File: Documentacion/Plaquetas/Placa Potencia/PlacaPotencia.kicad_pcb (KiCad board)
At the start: 2 copper layers, 31 parts, among them J1 Conn_01x02_Male, Q1 IRF4905, Q2 IRFZ44N, Q3 IRF4905, Q4 IRFZ44N, Q5 BC337, Q6 BC337, U2 MCP1407, U3 MCP1407

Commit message: Power PCB Routed
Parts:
- added C_MCP1: 10n, Capacitor_THT:C_Rect_L7.5mm_W6.5mm_P5.00mm, F.Cu at (133.0, 44.5)
- added C_MCP2: 10n, Capacitor_THT:C_Rect_L7.5mm_W6.5mm_P5.00mm, F.Cu at (234.0, 63.0)
- moved BORNERA3 70.4 mm to (129.5, 83.5), turned to 180 degrees
- moved BORNERA2 68.9 mm to (129.5, 78.0), turned to 180 degrees
- moved PELTIER1 36.6 mm to (187.5, 45.0)
- moved C4 35.6 mm to (130.0, 67.0), turned to 180 degrees
- moved R22 30.8 mm to (209.0, 89.0), turned to 270 degrees
- moved R2 30.6 mm to (130.1, 63.0), turned to 180 degrees
- moved D1 26.4 mm to (196.5, 82.5), turned to 0 degrees
- moved R14 21.8 mm to (141.0, 60.1)
- moved Q4 21.5 mm to (151.5, 52.5)
- moved Q5 21.5 mm to (142.5, 54.5)
- moved R21 20.6 mm to (143.0, 70.5)
- moved U2 20.2 mm to (130.5, 53.0), turned to 90 degrees
- moved D3 20.0 mm to (173.5, 82.5), turned to 180 degrees
- moved D4 16.6 mm to (156.0, 57.0), turned to 0 degrees
- moved D2 14.7 mm to (220.5, 69.5)
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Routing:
- net GND: track 225.6 -> 353.7 mm, vias 0 -> 2
- net PWM_FRIO: track 126.6 -> 21.0 mm, vias 1 -> 0
- net PMOS_FRIO: track 92.0 -> 22.7 mm, vias 1 -> 2
- net PWM_CALOR: track 86.2 -> 130.6 mm, vias 1 -> 2
- net PMOS_CALOR: track 98.5 -> 131.4 mm, vias 1 -> 2
- net Net-(R22-Pad2): track 35.0 -> 64.1 mm
- net Net-(Q2-Pad1): track 54.1 -> 31.0 mm
- net Net-(Q1-Pad1): track 165.6 -> 184.3 mm, vias 1 -> 2
- net Net-(C2-Pad1): track 30.1 -> 44.1 mm
- net Net-(Q3-Pad1): track 137.6 -> 123.8 mm
- net VCC: track 522.7 -> 509.4 mm
- net Net-(C1-Pad1): track 35.2 -> 44.5 mm
- net Net-(R21-Pad2): track 33.7 -> 41.5 mm
- net Net-(Q4-Pad1): track 26.4 -> 21.5 mm
- net Net-(D1-Pad2): track 39.6 -> 43.2 mm
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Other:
- board outline added: 145 x 70 mm

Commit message: Power PCB revised
Minor changes in size and vias
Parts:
- moved J1 70.1 mm to (75.0, 42.5)
- moved R22 31.3 mm to (204.5, 58.0)
- moved R11 7.50 mm to (144.0, 82.5)
- moved BORNERA2 5.50 mm to (135.0, 78.0)
- moved BORNERA3 5.50 mm to (135.0, 83.5)
- moved C2 5.50 mm to (184.0, 69.5)
- moved C4 5.50 mm to (135.5, 67.0)
- moved C_MCP1 5.50 mm to (138.5, 44.5)
- moved D3 5.50 mm to (179.0, 82.5)
- moved D4 5.50 mm to (161.5, 57.0)
- moved L2 5.50 mm to (164.0, 69.5)
- moved Q3 5.50 mm to (153.5, 83.0)
- moved Q4 5.50 mm to (157.0, 52.5)
- moved Q5 5.50 mm to (148.0, 54.5)
- moved R14 5.50 mm to (146.5, 60.1)
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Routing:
- net Net-(Q2-Pad1): track 31.0 -> 4.50 mm
- net GND: track 353.7 -> 369.7 mm, vias 2 -> 0
- net Net-(R22-Pad2): track 64.1 -> 52.6 mm, vias 0 -> 1
- net PMOS_CALOR: track 131.4 -> 125.1 mm, vias 2 -> 1
- net Net-(Q3-Pad1): track 123.8 -> 118.3 mm
- net PWM_CALOR: track 130.6 -> 125.1 mm, vias 2 -> 1
- net VCC: track 509.4 -> 504.9 mm
- net Net-(C2-Pad1): track 44.1 -> 45.5 mm
- net Net-(Q1-Pad1): track 184.3 -> 183.5 mm, vias 2 -> 1
- net PMOS_FRIO: track 22.7 -> 22.3 mm, vias 2 -> 1

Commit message: Power PCB footprints updated
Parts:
- removed BORNERA2, BORNERA3: Screw_Terminal_01x02, Connector_PinHeader_2.54mm:PinHeader_1x02_P2.54mm_Vertical
- added C10: 4.7u, Capacitor_THT:C_Rect_L29.0mm_W9.1mm_P27.50mm_MKT, F.Cu at (21.8, 163.8)
- added C11: 4.7u, Capacitor_THT:C_Rect_L29.0mm_W9.1mm_P27.50mm_MKT, F.Cu at (84.7, 131.8)
- added C12: 4.7u, Capacitor_THT:C_Rect_L29.0mm_W9.1mm_P27.50mm_MKT, F.Cu at (21.8, 174.4)
- added C13: 4.7u, Capacitor_THT:C_Rect_L29.0mm_W9.1mm_P27.50mm_MKT, F.Cu at (53.2, 153.1)
- added C14: 4.7u, Capacitor_THT:C_Rect_L29.0mm_W9.1mm_P27.50mm_MKT, F.Cu at (84.7, 142.5)
- added C15: 4.7u, Capacitor_THT:C_Rect_L29.0mm_W9.1mm_P27.50mm_MKT, F.Cu at (53.2, 163.8)
- added C16: 4.7u, Capacitor_THT:C_Rect_L29.0mm_W9.1mm_P27.50mm_MKT, F.Cu at (53.2, 174.4)
- added C5: 4.7u, Capacitor_THT:C_Rect_L29.0mm_W9.1mm_P27.50mm_MKT, F.Cu at (21.8, 131.8)
- added C6: 4.7u, Capacitor_THT:C_Rect_L29.0mm_W9.1mm_P27.50mm_MKT, F.Cu at (21.8, 142.5)
- added C7: 4.7u, Capacitor_THT:C_Rect_L29.0mm_W9.1mm_P27.50mm_MKT, F.Cu at (53.2, 131.8)
- added C8: 4.7u, Capacitor_THT:C_Rect_L29.0mm_W9.1mm_P27.50mm_MKT, F.Cu at (21.8, 153.1)
- added C9: 4.7u, Capacitor_THT:C_Rect_L29.0mm_W9.1mm_P27.50mm_MKT, F.Cu at (53.2, 142.5)
- added J2: Conn_01x10_Male, Connector_IDC:IDC-Header_2x05_P2.54mm_Vertical, F.Cu at (101.5, 114.5)
- C1: value 33uF -> 1u; footprint Capacitor_THT:CP_Radial_D13.0mm_P7.50mm -> Capacitor_THT:C_Rect_L16.5mm_W10.7mm_P15.00mm_MKT
- C2: value 33uF -> 1000u; footprint Capacitor_THT:CP_Radial_D13.0mm_P7.50mm -> Capacitor_THT:CP_Radial_D10.0mm_P5.00mm
- C_MCP1, C_MCP2: value 10n -> 680n; footprint Capacitor_THT:C_Rect_L7.5mm_W6.5mm_P5.00mm -> custom_footprints:C_Rect_L21.5mm_W5.5mm_P20.00mm_MKS4
- R21, R22: footprint Resistor_THT:R_Axial_DIN0204_L3.6mm_D1.6mm_P5.08mm_Horizontal -> Resistor_THT:R_Axial_DIN0411_L9.9mm_D3.6mm_P12.70mm_Horizontal
- moved C1 136.2 mm to (84.6, 153.9)
- moved C2 115.4 mm to (105.0, 153.6), turned to 0 degrees
- moved C_MCP1 43.6 mm to (141.0, 88.0), turned to 90 degrees
- moved C_MCP2 41.6 mm to (245.5, 103.0)
- moved C3 30.0 mm to (226.5, 89.5)
- moved C4 30.0 mm to (135.5, 97.0)
- moved D1 30.0 mm to (196.5, 112.5)
- moved D2 30.0 mm to (220.5, 99.5)
- moved D3 30.0 mm to (179.0, 112.5)
- moved D4 30.0 mm to (161.5, 87.0)
- moved L1 30.0 mm to (206.5, 99.5)
- moved L2 30.0 mm to (164.0, 99.5)
- moved Q1 30.0 mm to (224.5, 110.5)
- moved Q2 30.0 mm to (209.0, 88.0)
- moved Q3 30.0 mm to (153.5, 113.0)
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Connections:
- C1 pad 1: Net-(C1-Pad1) -> VCC
- C2 pad 1: Net-(C2-Pad1) -> VCC
- L1 pad 1: Net-(C1-Pad1) -> PELTIER1
- L2 pad 2: Net-(C2-Pad1) -> PELTIER2
- PELTIER1 pad 1: Net-(C1-Pad1) -> PELTIER1
- PELTIER1 pad 2: Net-(C2-Pad1) -> PELTIER2
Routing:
- net PELTIER2: track 0.00 -> 45.5 mm
- net Net-(C2-Pad1): track 45.5 -> 0.00 mm
- net PELTIER1: track 0.00 -> 44.5 mm
- net Net-(C1-Pad1): track 44.5 -> 0.00 mm
- net GND: track 369.7 -> 328.4 mm
- net VCC: track 504.9 -> 472.6 mm
- net PWM_FRIO: track 21.0 -> 11.7 mm
- net Net-(R22-Pad2): track 52.6 -> 59.6 mm
- net Net-(Q2-Pad1): track 4.50 -> 10.4 mm
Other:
- board size 145 x 70 mm -> 145 x 100 mm

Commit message: Power PCB retraced routes for new footprints
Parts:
- moved C5 230.4 mm to (239.5, 56.5), turned to 270 degrees
- moved C1 202.8 mm to (253.0, 41.0), turned to 270 degrees
- moved C7 191.7 mm to (229.5, 56.5), turned to 270 degrees
- moved C6 188.6 mm to (179.5, 39.0), turned to 270 degrees
- moved C9 187.2 mm to (219.5, 56.5), turned to 270 degrees
- moved C8 186.7 mm to (169.5, 39.0), turned to 270 degrees
- moved C12 186.1 mm to (149.5, 39.0), turned to 270 degrees
- moved C10 185.8 mm to (159.5, 39.0), turned to 270 degrees
- moved C13 175.3 mm to (199.5, 56.5), turned to 270 degrees
- moved C15 173.4 mm to (189.5, 56.5), turned to 270 degrees
- moved C2 167.5 mm to (229.0, 41.0), turned to 270 degrees
- moved C16 155.4 mm to (129.5, 39.0), turned to 270 degrees
- moved C11 145.8 mm to (209.5, 56.5), turned to 270 degrees
- moved C14 117.1 mm to (139.5, 39.0), turned to 270 degrees
- moved J1 45.5 mm to (112.0, 69.0), turned to 90 degrees
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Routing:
- net GND: track 328.4 -> 595.6 mm
- net PELTIER1: track 44.5 -> 144.1 mm
- net PELTIER2: track 45.5 -> 139.8 mm
- net VCC: track 472.6 -> 537.4 mm
- net Net-(D1-Pad2): track 43.2 -> 63.4 mm
- net Net-(Q3-Pad1): track 118.3 -> 137.2 mm
- net PMOS_CALOR: track 125.1 -> 137.7 mm
- net PWM_FRIO: track 11.7 -> 22.2 mm
- net PWM_CALOR: track 125.1 -> 117.4 mm
- net Net-(R21-Pad2): track 41.5 -> 34.6 mm
- net Net-(Q1-Pad1): track 183.5 -> 187.2 mm
- net Net-(Q4-Pad1): track 21.5 -> 19.4 mm
- net Net-(R22-Pad2): track 59.6 -> 60.6 mm
- net Net-(Q5-Pad2): track 5.98 -> 6.66 mm

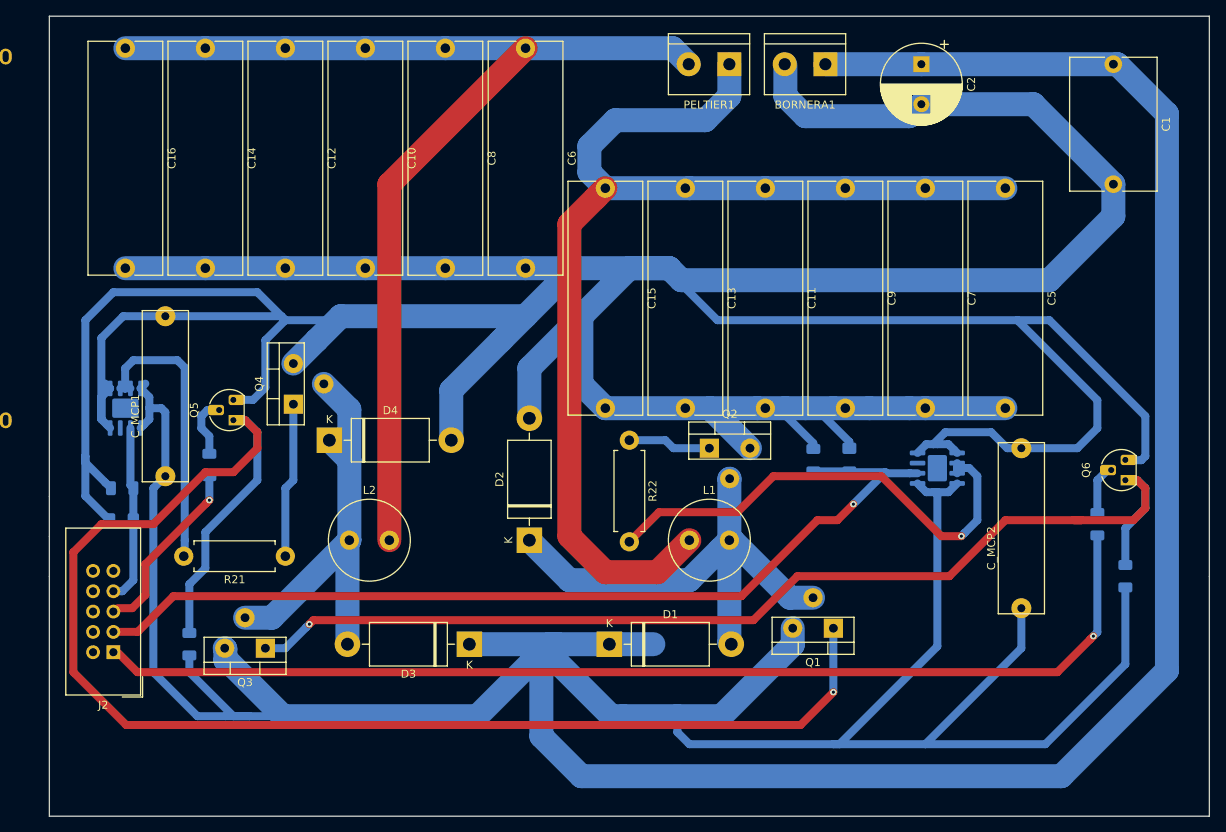
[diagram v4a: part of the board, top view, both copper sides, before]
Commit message: Power PCB complete route retracing
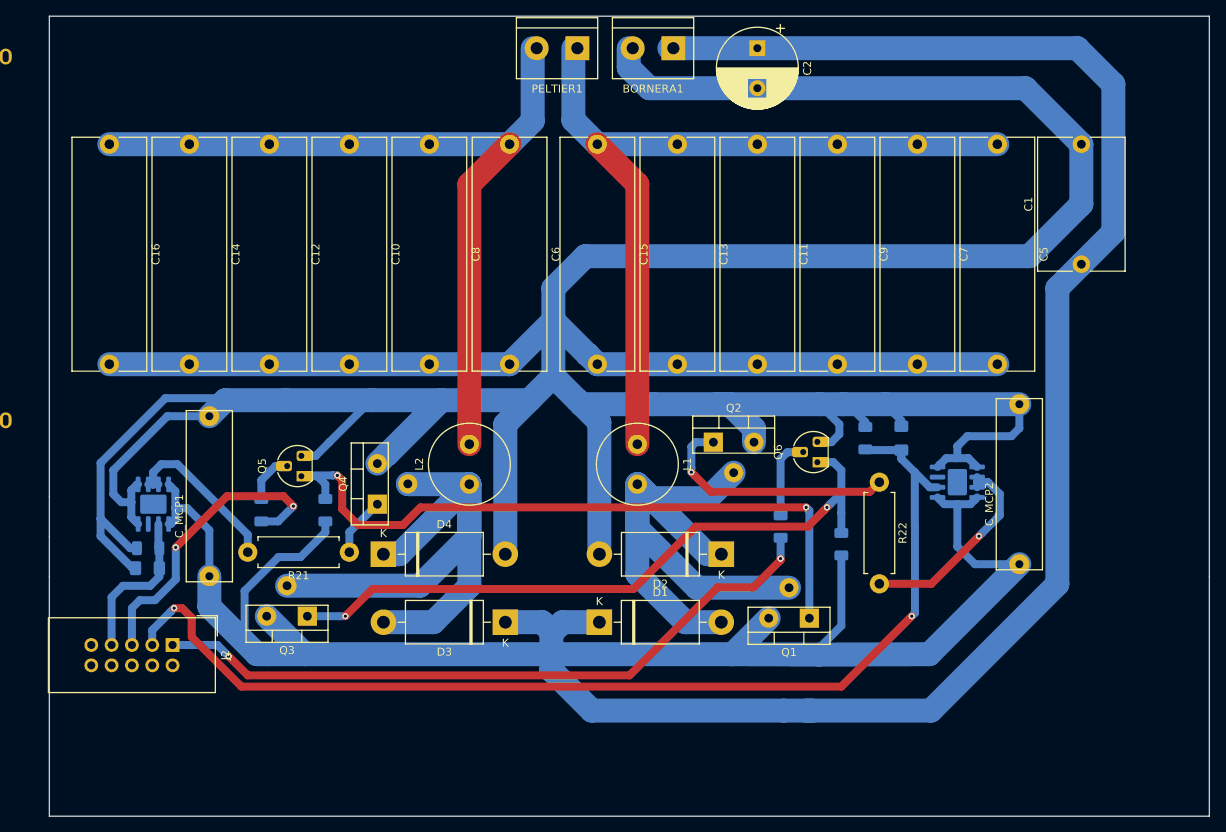
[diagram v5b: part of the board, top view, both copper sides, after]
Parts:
- moved R15 39.6 mm to (211.4, 98.8)
- moved Q6 38.6 mm to (215.5, 90.8)
- moved R12 35.7 mm to (219.0, 101.0)
- moved R22 31.7 mm to (223.8, 93.2)
- moved C1 25.3 mm to (249.0, 66.0), turned to 90 degrees
- moved D2 24.1 mm to (204.0, 102.2), turned to 180 degrees
- moved R11 23.9 mm to (154.5, 96.8)
- moved C2 20.6 mm to (208.5, 39.0)
- moved BORNERA1 19.1 mm to (198.0, 39.0)
- moved PELTIER1 19.1 mm to (186.0, 39.0)
- moved L2 16.6 mm to (172.5, 93.5), turned to 90 degrees
- moved Q4 16.3 mm to (161.0, 96.0)
- moved D4 15.8 mm to (161.8, 102.2)
- moved C_MCP1 13.7 mm to (140.0, 105.0)
- moved L1 13.6 mm to (193.5, 88.5), turned to 270 degrees
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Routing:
- net VCC: track 537.4 -> 412.1 mm
- net Net-(Q1-Pad1): track 187.2 -> 88.0 mm, vias 1 -> 2
- net Net-(Q3-Pad1): track 137.2 -> 84.4 mm, vias 1 -> 2
- net PMOS_CALOR: track 137.7 -> 86.3 mm, vias 1 -> 2
- net PELTIER1: track 144.1 -> 102.8 mm
- net PELTIER2: track 139.8 -> 102.8 mm
- net GND: track 595.6 -> 560.2 mm
- net Net-(R22-Pad2): track 60.6 -> 26.0 mm
- net Net-(D3-Pad2): track 54.6 -> 79.3 mm
- net Net-(Q2-Pad1): track 10.4 -> 31.2 mm, vias 0 -> 1
- net PWM_CALOR: track 117.4 -> 136.8 mm, vias 1 -> 2
- net Net-(D1-Pad2): track 63.4 -> 80.0 mm
- net PMOS_FRIO: track 22.3 -> 38.2 mm, vias 1 -> 2
- net Net-(R21-Pad2): track 34.6 -> 20.9 mm
- net Net-(Q4-Pad1): track 19.4 -> 7.45 mm
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
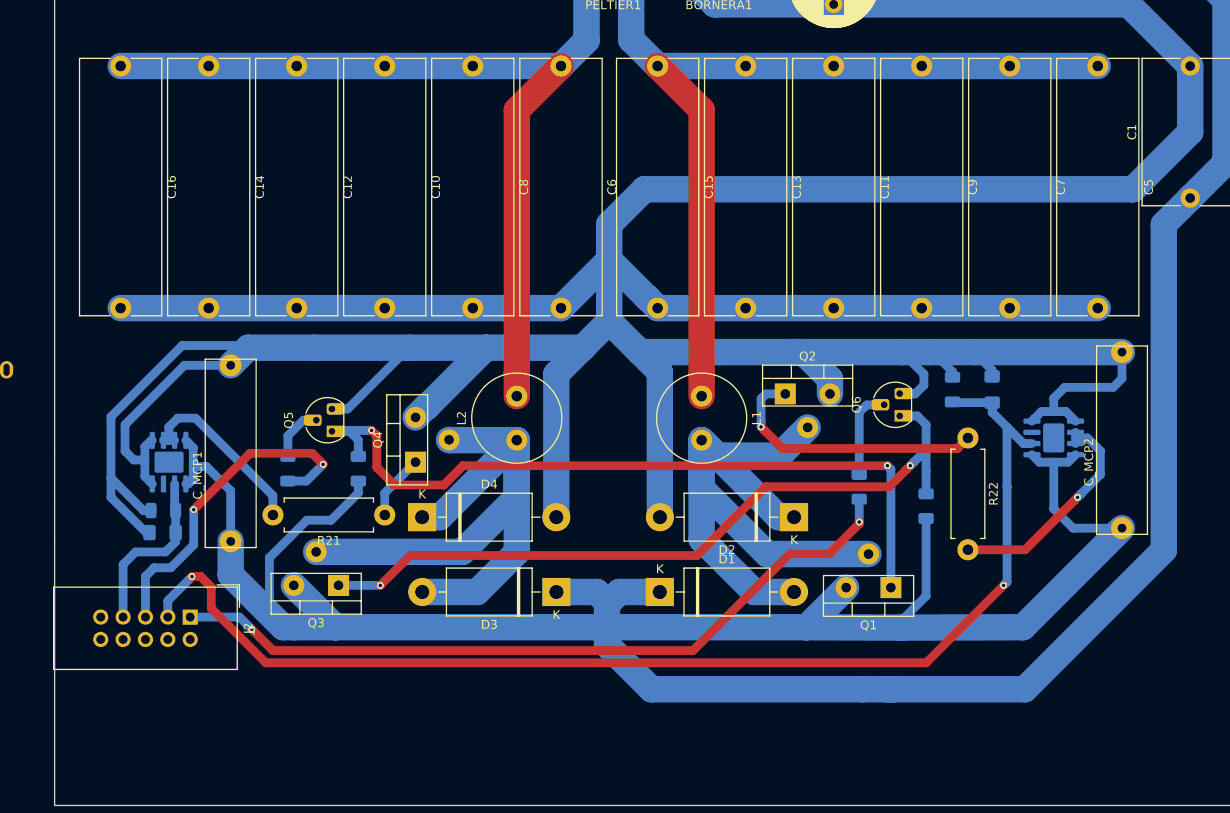
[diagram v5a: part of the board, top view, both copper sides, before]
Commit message: Power PCB revision - via size, signal connector pos and front pow traces
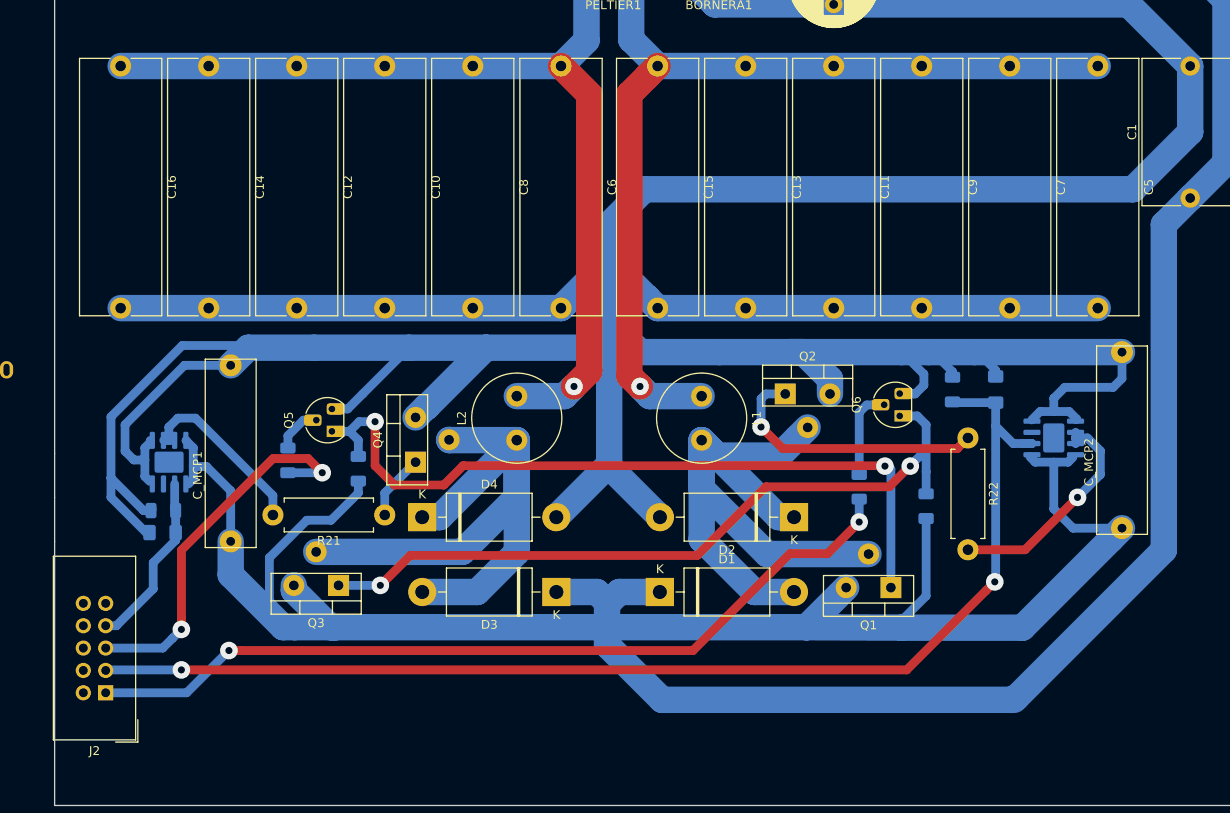
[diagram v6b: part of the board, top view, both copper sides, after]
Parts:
- moved J2 12.9 mm to (125.8, 122.2), turned to 180 degrees
- moved R14 0.95 mm to (146.5, 95.8)
- moved C3 0.40 mm to (226.9, 87.8)
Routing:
- net PMOS_CALOR: track 86.3 -> 96.2 mm
- net GND: track 560.2 -> 552.7 mm
- net PELTIER1: track 102.8 -> 108.9 mm, vias 0 -> 1
- net PELTIER2: track 102.8 -> 108.6 mm, vias 0 -> 1
- net PMOS_FRIO: track 38.2 -> 43.3 mm
- net Net-(Q5-Pad2): track 6.31 -> 5.36 mm
- net PWM_CALOR: track 136.8 -> 136.0 mm
- net PWM_FRIO: track 19.6 -> 20.2 mm
- net Net-(Q1-Pad1): track 88.0 -> 87.5 mm
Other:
- net class Default: clearance 0.2 -> 0.5
- rule trace_clearance: 0.2 -> 0.5
